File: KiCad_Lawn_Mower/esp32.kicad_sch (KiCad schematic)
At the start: 1 part, among them U2 ESP32-S3-DEVKITC-1U-N8R8

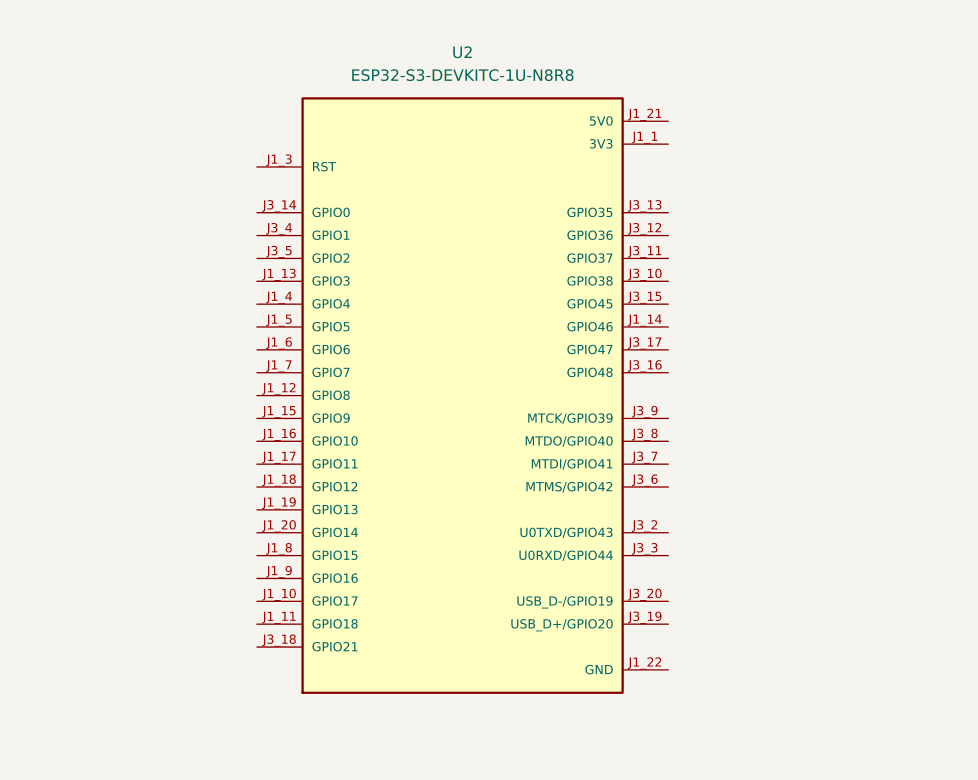
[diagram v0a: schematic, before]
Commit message: Update schematics and system design
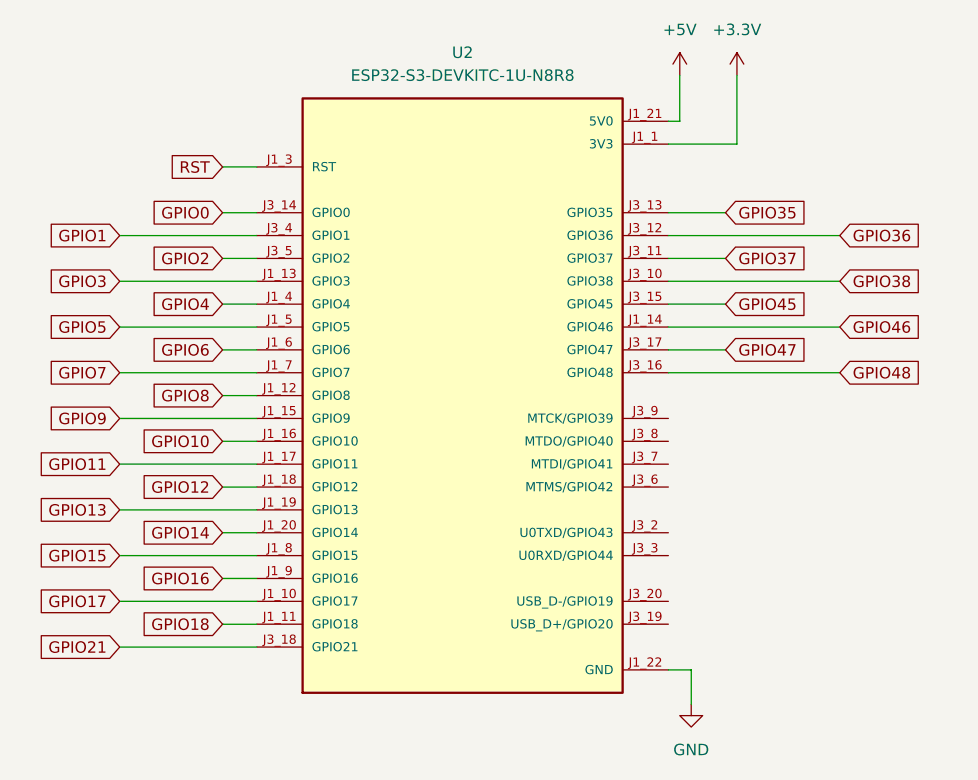
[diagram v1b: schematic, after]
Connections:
- net GPIO17: now reaches U2.J1_10 (GPIO17)
- net GPIO18: now reaches U2.J1_11 (GPIO18)
- net GPIO8: now reaches U2.J1_12 (GPIO8)
- net GPIO3: now reaches U2.J1_13 (GPIO3)
- net GPIO46: now reaches U2.J1_14 (GPIO46)
- net GPIO9: now reaches U2.J1_15 (GPIO9)
- net GPIO10: now reaches U2.J1_16 (GPIO10)
- net GPIO11: now reaches U2.J1_17 (GPIO11)
- net GPIO12: now reaches U2.J1_18 (GPIO12)
- net GPIO13: now reaches U2.J1_19 (GPIO13)
- net GPIO14: now reaches U2.J1_20 (GPIO14)
- net +5V: now reaches U2.J1_21 (5V0)
- net RST: now reaches U2.J1_3 (RST)
- net GPIO4: now reaches U2.J1_4 (GPIO4)
- net GPIO5: now reaches U2.J1_5 (GPIO5)
- net GPIO6: now reaches U2.J1_6 (GPIO6)
- net GPIO7: now reaches U2.J1_7 (GPIO7)
- net GPIO15: now reaches U2.J1_8 (GPIO15)
- net GPIO16: now reaches U2.J1_9 (GPIO16)
- net GPIO38: now reaches U2.J3_10 (GPIO38)
- net GPIO37: now reaches U2.J3_11 (GPIO37)
- net GPIO36: now reaches U2.J3_12 (GPIO36)
- net GPIO35: now reaches U2.J3_13 (GPIO35)
- net GPIO0: now reaches U2.J3_14 (GPIO0)
- net GPIO45: now reaches U2.J3_15 (GPIO45)
- net GPIO48: now reaches U2.J3_16 (GPIO48)
- net GPIO47: now reaches U2.J3_17 (GPIO47)
- net GPIO21: now reaches U2.J3_18 (GPIO21)
- net GPIO1: now reaches U2.J3_4 (GPIO1)
- net GPIO2: now reaches U2.J3_5 (GPIO2)
- net 3V3 renamed +3.3V

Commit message: Adding IR sensor init and fixing schematic
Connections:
- net GPIO35 renamed TAKEN_35
- net GPIO36 renamed TAKEN_36
- net GPIO37 renamed TAKEN_37
- net GPIO38 renamed TAKEN_38
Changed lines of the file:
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@@
 		)
 	)
-	(global_label "GPIO38"
+	(global_label "TAKEN_38"
 		(shape input)
 		(at 172.72 72.39 0)
@@
 		)
 		(property "Intersheetrefs" "${INTERSHEET_REFS}"
-			(at 182.5995 72.39 0)
+			(at 184.8975 72.39 0)
 			(hide yes)
 			(show_name no)
@@
 		)
 	)
-	(global_label "GPIO35"
+	(global_label "TAKEN_35"
 		(shape input)
 		(at 160.02 64.77 0)
@@
 		)
 		(property "Intersheetrefs" "${INTERSHEET_REFS}"
-			(at 169.8995 64.77 0)
+			(at 172.1975 64.77 0)
 			(hide yes)
 			(show_name no)
@@
 		)
 	)
-	(global_label "GPIO37"
+	(global_label "TAKEN_37"
 		(shape input)
 		(at 160.02 69.85 0)
@@
 		)
 		(property "Intersheetrefs" "${INTERSHEET_REFS}"
-			(at 169.8995 69.85 0)
+			(at 172.1975 69.85 0)
 			(hide yes)
 			(show_name no)
@@
 		)
 	)
-	(global_label "GPIO36"
+	(global_label "TAKEN_36"
 		(shape input)
 		(at 172.72 67.31 0)
@@
 		)
 		(property "Intersheetrefs" "${INTERSHEET_REFS}"
-			(at 182.5995 67.31 0)
-			(hide yes)
-			(show_name no)
+			(at 184.8975 67.31 0)
+			(hide yes)
+			(show_name no)
